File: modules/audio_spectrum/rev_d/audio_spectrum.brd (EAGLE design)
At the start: 68.1 x 66 mm, 107 parts, among them J1 AUDIO-JACK-VERTICAL, J2 MODULE_GENERIC_DEBUG, J3 TC2030-JLINK-L, P1 4k-200k, P2 4k-200k, Q1 NX3008PBK, Q2 NX3008PBK, U1 AT45DB641EUDFN, U10 TLV62130, U2 MP23AB02B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

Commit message: make audio rev_d four layer
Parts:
- C1, C2: device passives:0603_CAP -> passives:0402_CAP
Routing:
- added copper zone on layer 15, net 3V3
- added copper zone on layer 2, net GND
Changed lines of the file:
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@@
 <layers>
 <layer number="1" name="Top" color="4" fill="1" visible="yes" active="yes"/>
-<layer number="2" name="Route2" color="1" fill="3" visible="no" active="no"/>
+<layer number="2" name="Route2" color="1" fill="3" visible="yes" active="yes"/>
 <layer number="3" name="Route3" color="4" fill="3" visible="no" active="no"/>
 <layer number="4" name="Route4" color="1" fill="4" visible="no" active="no"/>
@@
 <layer number="13" name="Route13" color="4" fill="5" visible="no" active="no"/>
 <layer number="14" name="Route14" color="1" fill="6" visible="no" active="no"/>
-<layer number="15" name="Route15" color="4" fill="6" visible="no" active="no"/>
+<layer number="15" name="Route15" color="4" fill="6" visible="yes" active="yes"/>
 <layer number="16" name="Bottom" color="1" fill="1" visible="yes" active="yes"/>
 <layer number="17" name="Pads" color="2" fill="1" visible="yes" active="yes"/>
@@
 </class>
 </classes>
-<designrules name="quickturn_co_kr_1oz">
+<designrules name="quickturn_co_kr_1oz *">
 <description language="en">&lt;b&gt;EAGLE Design Rules for *2* Layer Designs (DS)&lt;/b&gt;
 &lt;p&gt;
@@
 &lt;p&gt;
 &lt;i&gt;Attention: Upon running the design check and making modifications, please remember to save any changes before closing the application and sending in your board file to Sunstone Circuits for conversion.&lt;i&gt;</description>
-<param name="layerSetup" value="(1*16)"/>
+<param name="layerSetup" value="(1+2*15+16)"/>
 <param name="mtCopper" value="0.0178mm 0.0356mm 0.0356mm 0.0356mm 0.0356mm 0.0356mm 0.0356mm 0.0356mm 0.0356mm 0.0356mm 0.0356mm 0.0356mm 0.0356mm 0.0356mm 0.0356mm 0.0178mm"/>
-<param name="mtIsolate" value="59mil 0.1499mm 0.2007mm 0.1499mm 0.2007mm 0.1499mm 0.2007mm 0.1499mm 0.2007mm 0.1499mm 0.2007mm 0.1499mm 0.2007mm 0.1499mm 0.2007mm"/>
+<param name="mtIsolate" value="12mil 28mil 0.2007mm 0.1499mm 0.2007mm 0.1499mm 0.2007mm 0.1499mm 0.2007mm 0.1499mm 0.2007mm 0.1499mm 0.2007mm 0.1499mm 12mil"/>
 <param name="mdWireWire" value="4mil"/>
 <param name="mdWirePad" value="4mil"/>
@@
 <attribute name="NAME" x="65.4304" y="38.1" size="0.889" layer="25" font="vector" ratio="12" align="bottom-center"/>
 </element>
-<element name="C1" library="passives" package="0603_CAP" value="8pF" x="47.5234" y="38.4048" smashed="yes" rot="R180">
-<attribute name="DIGIKEY" value="478-1215-1-ND" x="67.8434" y="15.5448" size="1.778" layer="27" font="vector" ratio="12" rot="R180" display="off"/>
+<element name="C1" library="passives" package="0402_CAP" value="8pF" x="47.5234" y="38.4048" smashed="yes" rot="R180">
+<attribute name="DIGIKEY" value="490-8230-1-ND" x="67.8434" y="15.5448" size="1.778" layer="27" font="vector" ratio="12" rot="R180" display="off"/>
 <attribute name="NAME" x="47.5488" y="38.9636" size="0.889" layer="25" font="vector" ratio="12" align="bottom-center"/>
 </element>
-<element name="C2" library="passives" package="0603_CAP" value="8pF" x="44.45" y="37.338" smashed="yes" rot="R90">
-<attribute name="DIGIKEY" value="478-1215-1-ND" x="26.67" y="11.938" size="1.778" layer="27" font="vector" ratio="12" rot="R90" display="off"/>
+<element name="C2" library="passives" package="0402_CAP" value="8pF" x="44.45" y="37.338" smashed="yes" rot="R90">
+<attribute name="DIGIKEY" value="490-8230-1-ND" x="26.67" y="11.938" size="1.778" layer="27" font="vector" ratio="12" rot="R90" display="off"/>
 <attribute name="NAME" x="44.3992" y="38.5318" size="0.889" layer="25" font="vector" ratio="12" align="bottom-center"/>
 </element>
@@
 <wire x1="33.6804" y1="55.2704" x2="34.29" y2="54.6608" width="0.254" layer="1"/>
 <wire x1="34.29" y1="54.6608" x2="34.29" y2="53.9543" width="0.254" layer="1"/>
+<polygon width="0.254" layer="2" isolate="0.1524" rank="2">
+<vertex x="2.032" y="75.692"/>
+<vertex x="79.502" y="75.692"/>
+<vertex x="79.502" y="-3.302"/>
+<vertex x="2.032" y="-3.302"/>
+</polygon>
 </signal>
 <signal name="AUDIO_SWDCLK">
@@
 <contactref element="U9" pad="1"/>
 <wire x1="48.434" y1="32.8838" x2="48.6118" y2="32.8838" width="0.254" layer="1"/>
-<wire x1="48.1734" y1="38.4048" x2="48.042" y2="38.2734" width="0.254" layer="1"/>
+<wire x1="47.95646875" y1="38.4048" x2="48.042" y2="38.2734" width="0.254" layer="1"/>
 <wire x1="48.042" y1="38.2734" x2="48.042" y2="36.843" width="0.254" layer="1"/>
 <wire x1="49.022" y1="34.5818" x2="49.022" y2="36.322" width="0.254" layer="1"/>
@@
 <wire x1="47.6262" y1="32.3838" x2="46.192" y2="33.818" width="0.254" layer="1"/>
 <wire x1="46.192" y1="33.818" x2="46.192" y2="35.293" width="0.254" layer="1"/>
-<wire x1="44.45" y1="36.688" x2="45.845" y2="35.293" width="0.254" layer="1"/>
+<wire x1="44.45" y1="36.90493125" x2="45.845" y2="35.293" width="0.254" layer="1"/>
 <wire x1="45.845" y1="35.293" x2="46.192" y2="35.293" width="0.254" layer="1"/>
 </signal>
@@
 <wire x1="24.3332" y1="38.2524" x2="32.893" y2="38.2524" width="0.508" layer="16"/>
 <wire x1="40.8432" y1="38.1762" x2="42.8244" y2="40.132" width="0.508" layer="16"/>
+<polygon width="0.254" layer="15" isolate="0.1524" rank="2">
+<vertex x="1.524" y="76.2"/>
+<vertex x="80.518" y="76.2"/>
+<vertex x="80.518" y="-4.064"/>
+<vertex x="1.524" y="-4.064"/>
+</polygon>
 </signal>
 <signal name="N$6">

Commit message: swapped SO/SI and add test points for flash chip
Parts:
- added !CS, SCLK, SI, SO: TEST_POINT_0.040IN, headers:TESTPOINT_0.040IN
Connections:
- net !FLASH_CS: now also !CS.TESTPOINT
- net FLASH_SCLK: now also SCLK.TESTPOINT
- net FLASH_SI: now also SI.TESTPOINT, U9.47; no longer U9.46
- net FLASH_SO: now also SO.TESTPOINT, U9.46; no longer U9.47
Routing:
- net FLASH_SCLK: track 5.38 -> 21.3 mm, vias 0 -> 2
- net FLASH_SI: track 5.14 -> 10.2 mm
- net !FLASH_CS: track 10.1 -> 14.3 mm
- net FLASH_SO: track 11.0 -> 14.1 mm, vias 0 -> 2
- net AUDIO_SWDIO: track 75.4 -> 78.4 mm

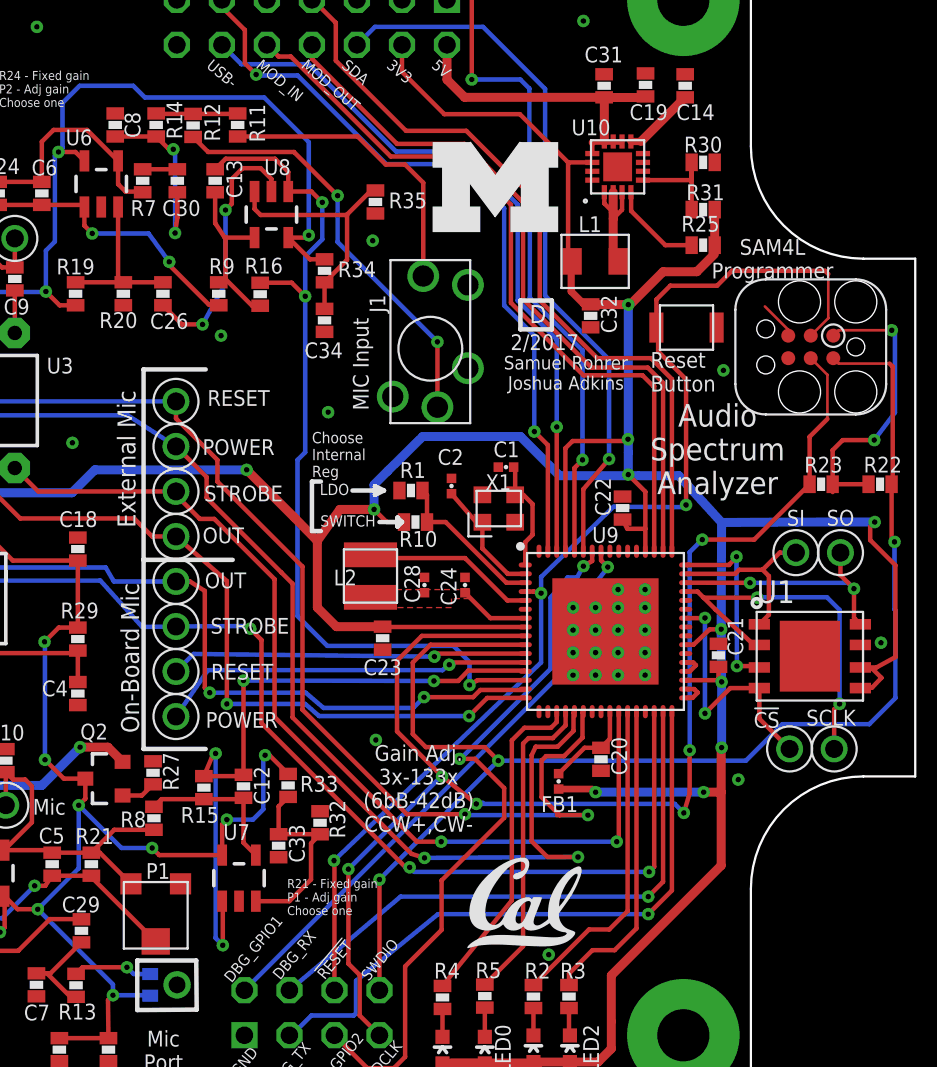
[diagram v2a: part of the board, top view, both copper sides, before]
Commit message: Re-ran gerbers after fixing error
DRC wasn't set up with proper clearance for the inner layers
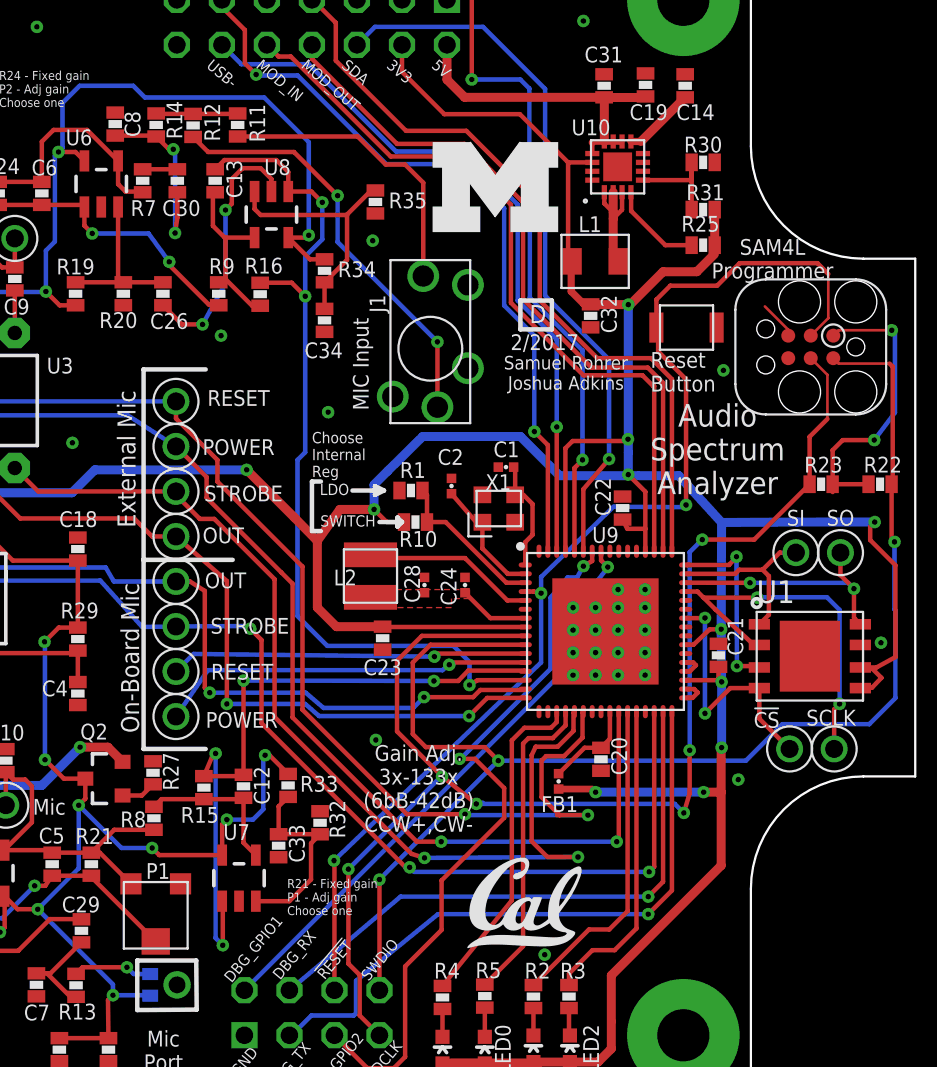
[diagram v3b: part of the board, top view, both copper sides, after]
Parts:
- moved C8 0.05 mm to (25.5, 57.8)
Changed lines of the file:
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@@
 <param name="mdDrill" value="16mil"/>
 <param name="mdSmdStop" value="0mil"/>
-<param name="msWidth" value="4mil"/>
-<param name="msDrill" value="0.200659375mm"/>
+<param name="msWidth" value="6mil"/>
+<param name="msDrill" value="8mil"/>
 <param name="msMicroVia" value="9.9898mm"/>
 <param name="msBlindViaRatio" value="0.5"/>
@@
 <param name="rlMinPadTop" value="8mil"/>
 <param name="rlMaxPadTop" value="999mil"/>
-<param name="rlMinPadInner" value="0mil"/>
-<param name="rlMaxPadInner" value="0mil"/>
+<param name="rlMinPadInner" value="8mil"/>
+<param name="rlMaxPadInner" value="999mil"/>
 <param name="rlMinPadBottom" value="8mil"/>
 <param name="rlMaxPadBottom" value="999mil"/>
 <param name="rlMinViaOuter" value="8mil"/>
 <param name="rlMaxViaOuter" value="999mil"/>
-<param name="rlMinViaInner" value="0mil"/>
-<param name="rlMaxViaInner" value="0mil"/>
+<param name="rlMinViaInner" value="8mil"/>
+<param name="rlMaxViaInner" value="999mil"/>
 <param name="rlMinMicroViaOuter" value="8mil"/>
 <param name="rlMaxMicroViaOuter" value="999mil"/>
-<param name="rlMinMicroViaInner" value="0mil"/>
-<param name="rlMaxMicroViaInner" value="0mil"/>
+<param name="rlMinMicroViaInner" value="8mil"/>
+<param name="rlMaxMicroViaInner" value="999mil"/>
 <param name="psTop" value="-1"/>
 <param name="psBottom" value="-1"/>
@@
 <param name="checkFont" value="1"/>
 <param name="checkRestrict" value="1"/>
-<param name="useDiameter" value="13"/>
+<param name="useDiameter" value="31"/>
 <param name="maxErrors" value="500"/>
 </designrules>
@@
 <attribute name="DIGIKEY" value="RHM10.0KHCT-ND" x="27.7876" y="57.7088" size="1.778" layer="27" rot="R270" display="off"/>
 </element>
-<element name="C8" library="passives" package="0603_CAP" value="360pF" x="25.4762" y="57.7088" smashed="yes" rot="R90">
-<attribute name="NAME" x="26.8986" y="57.7088" size="0.889" layer="25" font="vector" ratio="12" rot="R90" align="bottom-center"/>
-<attribute name="DIGIKEY" value="490-1440-1-ND" x="25.4762" y="57.7088" size="1.778" layer="27" rot="R90" display="off"/>
+<element name="C8" library="passives" package="0603_CAP" value="360pF" x="25.4762" y="57.7596" smashed="yes" rot="R90">
+<attribute name="NAME" x="26.8986" y="57.7596" size="0.889" layer="25" font="vector" ratio="12" rot="R90" align="bottom-center"/>
+<attribute name="DIGIKEY" value="490-1440-1-ND" x="25.4762" y="57.7596" size="1.778" layer="27" rot="R90" display="off"/>
 </element>
 <element name="U9" library="chips" package="QFN-64-9MM" value="SAM4LC8BA" x="53.1368" y="29.1338" smashed="yes">
@@
 <via x="40.1828" y="23.0124" extent="1-16" drill="0.3048"/>
 <via x="59.7916" y="43.8658" extent="1-16" drill="0.3048"/>
-<via x="49.9364" y="10.8966" extent="1-16" drill="0.3048"/>
+<via x="49.7078" y="10.8966" extent="1-16" drill="0.3048"/>
 <via x="9.8552" y="45.466" extent="1-16" drill="0.3048"/>
 <via x="21.0566" y="63.246" extent="1-16" drill="0.3048"/>
@@
 <wire x1="56.0088" y1="47.8554" x2="56.7944" y2="48.641" width="0.254" layer="1"/>
 <wire x1="56.7944" y1="48.641" x2="59.436" y2="48.641" width="0.254" layer="1"/>
-<wire x1="59.436" y1="48.641" x2="60.2742" y2="49.4792" width="0.254" layer="1"/>
+<wire x1="59.436" y1="48.641" x2="60.706" y2="49.911" width="0.254" layer="1"/>
 <wire x1="64.7192" y1="45.8216" x2="65.7098" y2="46.8122" width="0.1524" layer="1"/>
 <wire x1="65.7098" y1="46.8122" x2="65.7098" y2="49.3014" width="0.1524" layer="1"/>
-<wire x1="65.7098" y1="49.3014" x2="65.532" y2="49.4792" width="0.254" layer="1"/>
-<wire x1="65.532" y1="49.4792" x2="60.2742" y2="49.4792" width="0.254" layer="1"/>
+<wire x1="60.706" y1="49.911" x2="65.1002" y2="49.911" width="0.254" layer="1"/>
+<wire x1="65.1002" y1="49.911" x2="65.7098" y2="49.3014" width="0.254" layer="1"/>
 </signal>
 <signal name="AUDIO_XIN">
@@
 <contactref element="C30" pad="2"/>
 <contactref element="C8" pad="1"/>
-<wire x1="25.4762" y1="57.0588" x2="27.7876" y2="57.0588" width="0.254" layer="1"/>
 <wire x1="27.7876" y1="57.0588" x2="28.5092" y2="56.3372" width="0.254" layer="1"/>
 <wire x1="28.5092" y1="56.3372" x2="28.7528" y2="56.3372" width="0.254" layer="1"/>
@@
 <wire x1="28.9814" y1="53.9092" x2="28.9814" y2="52.4764" width="0.254" layer="1"/>
 <wire x1="28.9814" y1="52.4764" x2="28.8544" y2="51.6128" width="0.254" layer="1"/>
+<wire x1="25.4762" y1="57.1096" x2="27.7876" y2="57.1096" width="0.254" layer="1"/>
+<wire x1="27.7876" y1="57.1096" x2="27.7876" y2="57.0588" width="0.254" layer="1"/>
 </signal>
 <signal name="ADC_IN_MEMS">
@@
 <via x="37.1602" y="53.34" extent="1-16" drill="0.3048"/>
 <wire x1="35.24" y1="54.3966" x2="35.24" y2="53.9543" width="0.254" layer="1"/>
-<wire x1="31.115" y1="55.2092" x2="31.7096" y2="55.8038" width="0.254" layer="1"/>
-<wire x1="31.7096" y1="55.8038" x2="34.4932" y2="55.8038" width="0.254" layer="1"/>
-<wire x1="34.4932" y1="55.8038" x2="35.24" y2="55.057" width="0.254" layer="1"/>
+<wire x1="31.115" y1="55.2092" x2="31.636390625" y2="55.730590625" width="0.254" layer="1"/>
+<wire x1="31.636390625" y1="55.730590625" x2="34.566409375" y2="55.730590625" width="0.254" layer="1"/>
+<wire x1="34.566409375" y1="55.730590625" x2="35.24" y2="55.057" width="0.254" layer="1"/>
 <wire x1="35.24" y1="55.057" x2="35.24" y2="53.9543" width="0.254" layer="1"/>
 <wire x1="36.195" y1="39.243" x2="36.195" y2="48.0464" width="0.254" layer="16"/>
@@
 <wire x1="33.34" y1="51.3541" x2="31.6992" y2="51.3541" width="0.254" layer="1"/>
 <wire x1="31.6992" y1="51.3541" x2="31.6531" y2="51.3541" width="0.254" layer="1"/>
-<wire x1="31.6531" y1="51.3541" x2="31.115" y2="52.1716" width="0.254" layer="1"/>
-<wire x1="31.115" y1="52.1716" x2="31.115" y2="53.9092" width="0.254" layer="1"/>
 <wire x1="31.3182" y1="48.8338" x2="31.6992" y2="49.0116" width="0.254" layer="1"/>
 <wire x1="31.6992" y1="49.0116" x2="31.6992" y2="51.3541" width="0.254" layer="1"/>
 <wire x1="31.6992" y1="49.0116" x2="33.2024" y2="47.5084" width="0.254" layer="1"/>
 <wire x1="33.2024" y1="47.5084" x2="33.655" y2="47.5084" width="0.254" layer="1"/>
+<wire x1="30.988" y1="52.0192" x2="30.988" y2="53.7822" width="0.254" layer="1"/>
+<wire x1="30.988" y1="53.7822" x2="31.115" y2="53.9092" width="0.254" layer="1"/>
+<wire x1="30.988" y1="52.0192" x2="31.6531" y2="51.3541" width="0.254" layer="1"/>
 </signal>
 <signal name="N$22">
